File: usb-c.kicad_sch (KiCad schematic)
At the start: 37 parts, among them J2 USB-C_GCT_USB4105-GF-A, U12 FUSB303B, U13 AP22615B_TSOT26

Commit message: [#98577] Unify LEDs
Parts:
- D9: value LED_G_0603_LTST-C190GKT -> LED_G_0603_LG_L29K-G2J1-24-Z; symbol antmicroLEDIndicationDiscrete:LED_G_0603_LTST-C190GKT -> antmicroLEDIndicationDiscrete:LED_G_0603_LG_L29K-G2J1-24-Z; MPN LTST-C190GKT -> LG L29K-G2J1-24-Z; Manufacturer Lite-On -> OSRAM
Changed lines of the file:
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@@
 	)
 	(symbol
-		(lib_id "antmicroLEDIndicationDiscrete:LED_G_0603_LTST-C190GKT")
+		(lib_id "antmicroLEDIndicationDiscrete:LED_G_0603_LG_L29K-G2J1-24-Z")
 		(at 140.97 118.11 90)
 		(unit 1)
@@
 			)
 		)
-		(property "Value" "LED_G_0603_LTST-C190GKT"
-			(at 148.59 95.25 0)
+		(property "Value" "LED_G_0603_LG_L29K-G2J1-24-Z"
+			(at 148.59 97.79 0)
 			(effects
 				(font
@@
 		)
 		(property "Footprint" "antmicro-footprints:LED_0603_1608Metric_G"
-			(at 151.13 95.25 0)
+			(at 151.13 97.79 0)
 			(effects
 				(font
@@
 			)
 		)
-		(property "Datasheet" "https://media.digikey.com/pdf/Data%20Sheets/Lite-On%20PDFs/LTST-C190GKT.pdf"
-			(at 153.67 95.25 0)
+		(property "Datasheet" "https://look.ams-osram.com/m/19ee86b3ae0ee95b/original/LG-L29K.pdf"
+			(at 153.67 97.79 0)
 			(effects
 				(font
@@
 			)
 		)
-		(property "Description" "LED, Green, SMD, 0603, 20 mA, 2.1 V, 569 nm"
-			(at 166.37 95.25 0)
+		(property "Description" "LED, Green, SMD, 0603, 20 mA, 1.7 V, 570 nm"
+			(at 166.37 97.79 0)
 			(effects
 				(font
@@
 			)
 		)
-		(property "MPN" "LTST-C190GKT"
-			(at 156.21 95.25 0)
+		(property "MPN" "LG L29K-G2J1-24-Z"
+			(at 156.21 97.79 0)
 			(effects
 				(font
@@
 			)
 		)
-		(property "Manufacturer" "Lite-On"
-			(at 158.75 95.25 0)
+		(property "Manufacturer" "OSRAM"
+			(at 158.75 97.79 0)
 			(effects
 				(font
@@
 		)
 		(property "Author" "Antmicro"
-			(at 161.29 95.25 0)
+			(at 161.29 97.79 0)
 			(effects
 				(font
@@
 		)
 		(property "License" "Apache-2.0"
-			(at 163.83 95.25 0)
+			(at 163.83 97.79 0)
 			(effects
 				(font

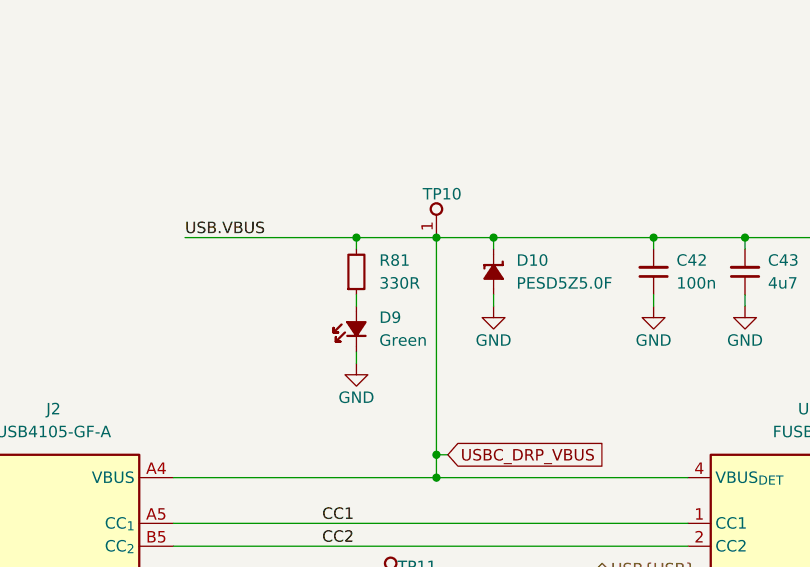
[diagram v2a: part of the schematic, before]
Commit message: [#98577] Unify LED Resistor values
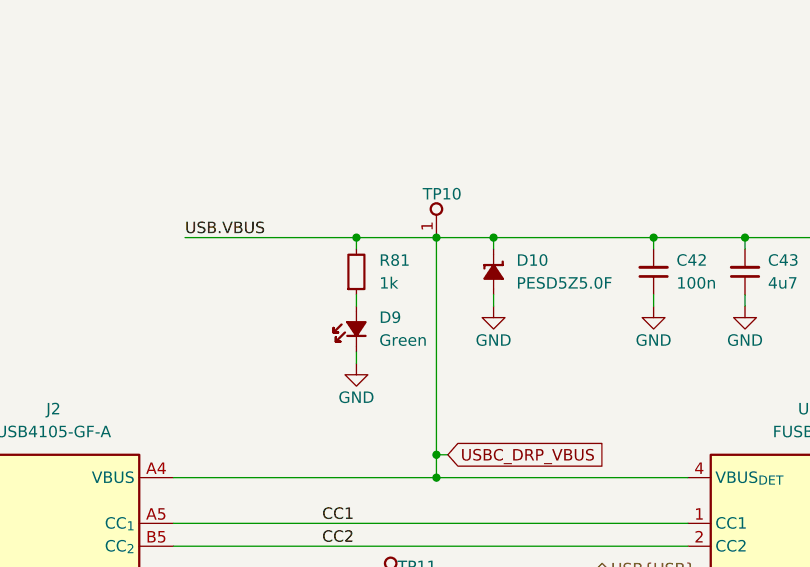
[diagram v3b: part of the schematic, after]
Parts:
- R81: value R_330R_0402 -> R_1k_0402; symbol antmicroResistors0402:R_330R_0402 -> antmicroResistors0402:R_1k_0402; MPN CR0402-FX-3300GLF -> CR0402-FX-1001GLF; Val 330R -> 1k
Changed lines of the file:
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@@
 	)
 	(symbol
-		(lib_id "antmicroResistors0402:R_330R_0402")
+		(lib_id "antmicroResistors0402:R_1k_0402")
 		(at 140.97 111.76 90)
 		(unit 1)
@@
 			)
 		)
-		(property "Value" "R_330R_0402"
+		(property "Value" "R_1k_0402"
 			(at 153.67 91.44 0)
 			(effects
@@
 			)
 		)
-		(property "Description" "SMD Chip Resistor, 330 ohm, ± 1%, 62.5 mW, 0402 [1005 Metric], Thick Film, General Purpose"
+		(property "Description" "SMD Chip Resistor, 1 kohm, ± 1%, 63 mW, 0402 [1005 Metric], Thick Film, General Purpose"
 			(at 171.45 91.44 0)
 			(effects
@@
 			)
 		)
-		(property "MPN" "CR0402-FX-3300GLF"
+		(property "MPN" "CR0402-FX-1001GLF"
 			(at 161.29 91.44 0)
 			(effects
@@
 			)
 		)
-		(property "Val" "330R"
+		(property "Val" "1k"
 			(at 143.51 110.49 90)
 			(effects
